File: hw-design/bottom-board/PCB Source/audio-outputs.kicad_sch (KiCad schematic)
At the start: 73 parts, among them J10 NYS215, J9 NYS215, K1 G6S-2, K2 G6S-2, Q1 2N7002, Q2 2N7002, U11 OPA1678, U12 OPA1678

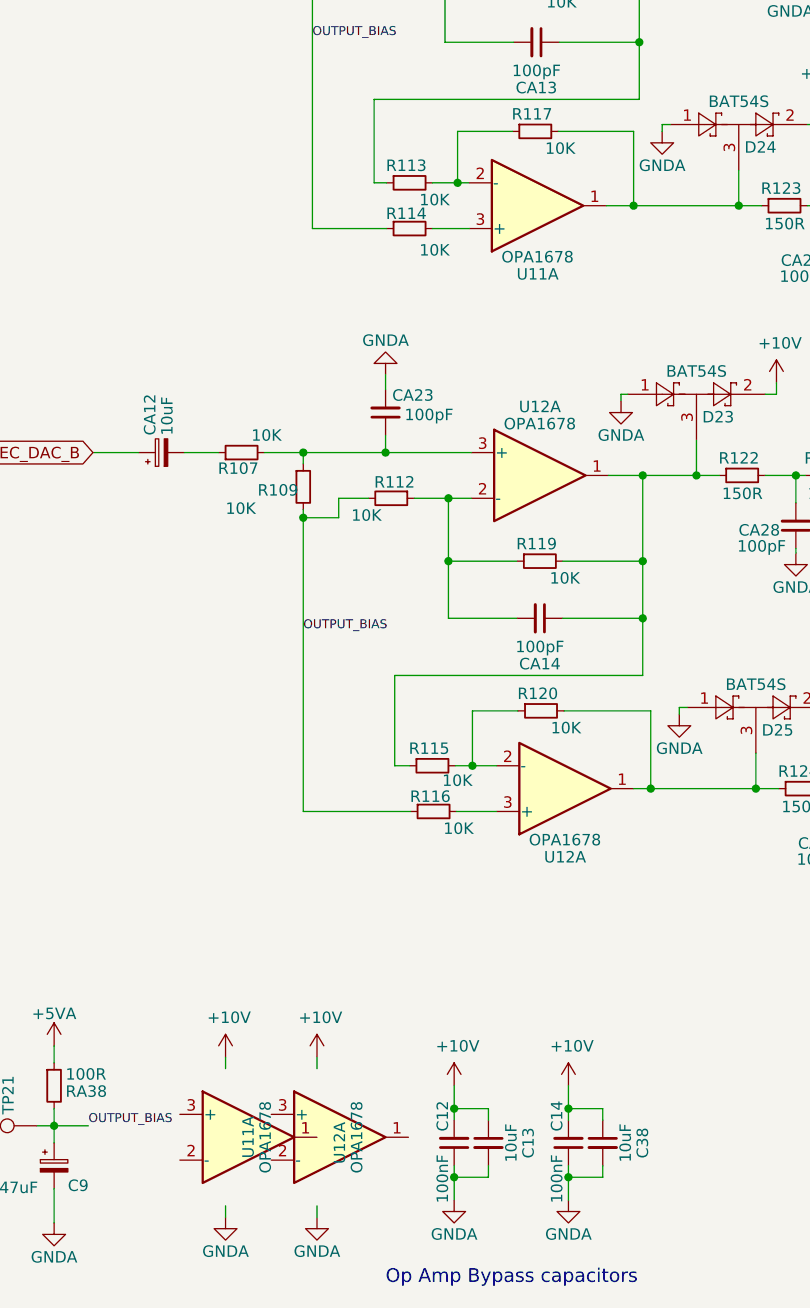
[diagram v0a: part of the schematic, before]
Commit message: change U21 (EXP supply) MPN, due to unavailabilaty again
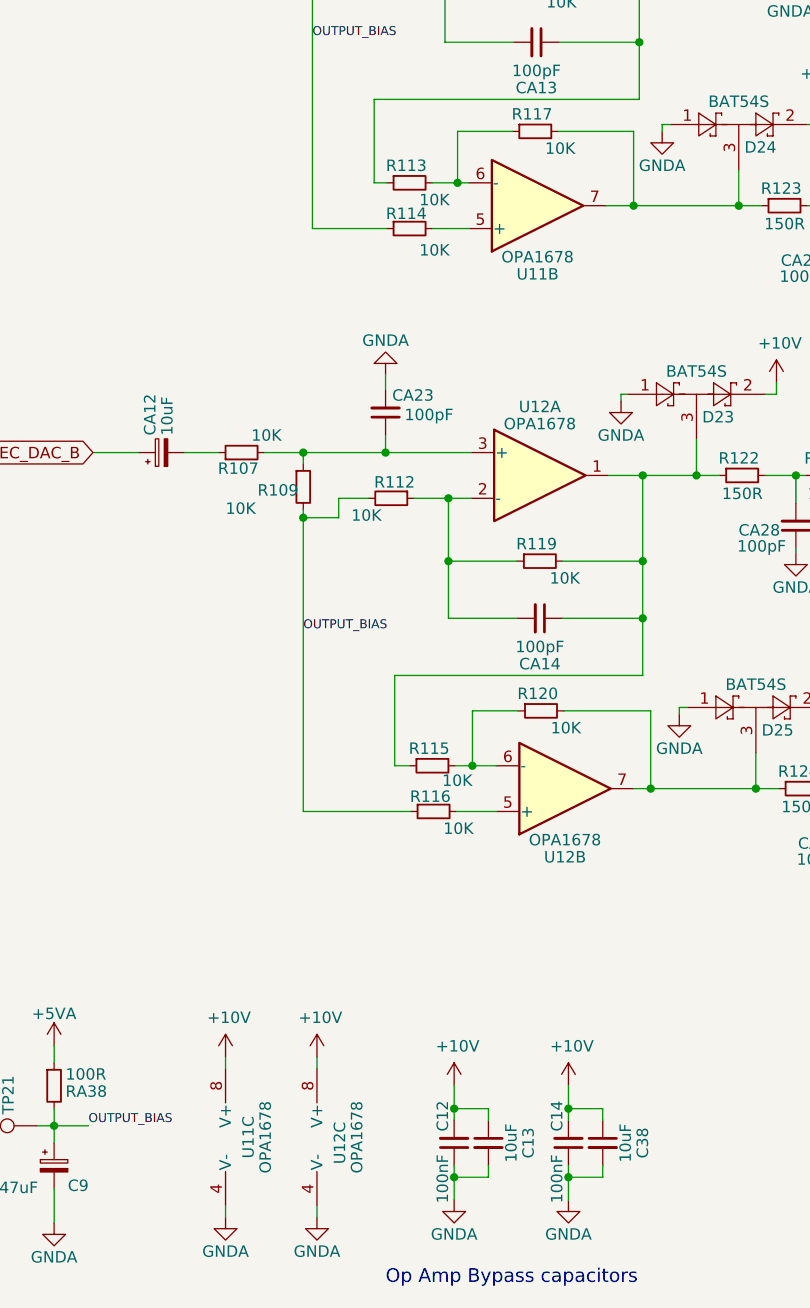
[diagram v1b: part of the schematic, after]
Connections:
- net +10V: now also U11.8 (V+), U12.8 (V+)
- net GNDA: now also U11.4 (V-), U12.4 (V-)
- net at D24.3, R117.2, R123.1: now also U11.7; no longer U11.1
- net at R113.2, R117.1: now also U11.6 (-); no longer U11.2 (-)
- net at R114.2: now also U11.5 (+); no longer U11.3 (+)
- net at D25.3, R120.2, R124.1: now also U12.7; no longer U12.1
- net at R115.2, R120.1: now also U12.6 (-); no longer U12.2 (-)
- net at R116.2: now also U12.5 (+); no longer U12.3 (+)
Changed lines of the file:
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@@
     (pin "3")
   )
-  (symbol (lib_id "bottom-board-rescue:LM4562-Amplifier_Operational") (at 45.085 168.91 0) (unit 1)
+  (symbol (lib_id "bottom-board-rescue:LM4562-Amplifier_Operational") (at 45.085 168.91 0) (unit 3)
     (in_bom yes) (on_board yes)
     (property "Reference" "U11" (id 0) (at 45.085 168.91 90))
@@
       (effects (font (size 1.27 1.27)) hide)
     )
-    (pin "1")
-    (pin "2")
-    (pin "3")
+    (pin "4")
+    (pin "8")
   )
   (symbol (lib_id "bottom-board-rescue:G6S-2-Relay") (at 154.813 108.077 90) (unit 1)
@@
     (pin "9")
   )
-  (symbol (lib_id "bottom-board-rescue:LM4562-Amplifier_Operational") (at 77.216 65.405 0) (mirror x) (unit 1)
+  (symbol (lib_id "bottom-board-rescue:LM4562-Amplifier_Operational") (at 77.216 65.405 0) (mirror x) (unit 2)
     (in_bom yes) (on_board yes)
     (property "Reference" "U11" (id 0) (at 77.216 73.025 0))
@@
       (effects (font (size 1.27 1.27)) hide)
     )
-    (pin "1")
-    (pin "2")
-    (pin "3")
+    (pin "5")
+    (pin "6")
+    (pin "7")
   )
-  (symbol (lib_id "bottom-board-rescue:LM4562-Amplifier_Operational") (at 55.245 168.91 0) (unit 1)
+  (symbol (lib_id "bottom-board-rescue:LM4562-Amplifier_Operational") (at 55.245 168.91 0) (unit 3)
     (in_bom yes) (on_board yes)
     (property "Reference" "U12" (id 0) (at 55.245 169.545 90))
@@
       (effects (font (size 1.27 1.27)) hide)
     )
-    (pin "1")
-    (pin "2")
-    (pin "3")
+    (pin "4")
+    (pin "8")
   )
   (symbol (lib_id "bottom-board-rescue:LM4562-Amplifier_Operational") (at 77.47 95.377 0) (unit 1)
@@
     (pin "3")
   )
-  (symbol (lib_id "bottom-board-rescue:LM4562-Amplifier_Operational") (at 80.264 130.175 0) (mirror x) (unit 1)
+  (symbol (lib_id "bottom-board-rescue:LM4562-Amplifier_Operational") (at 80.264 130.175 0) (mirror x) (unit 2)
     (in_bom yes) (on_board yes)
     (property "Reference" "U12" (id 0) (at 80.264 137.795 0))
@@
       (effects (font (size 1.27 1.27)) hide)
     )
-    (pin "1")
-    (pin "2")
-    (pin "3")
+    (pin "5")
+    (pin "6")
+    (pin "7")
   )
   (symbol (lib_id "bottom-board-rescue:R_Small-Device") (at 46.99 28.829 90) (unit 1)

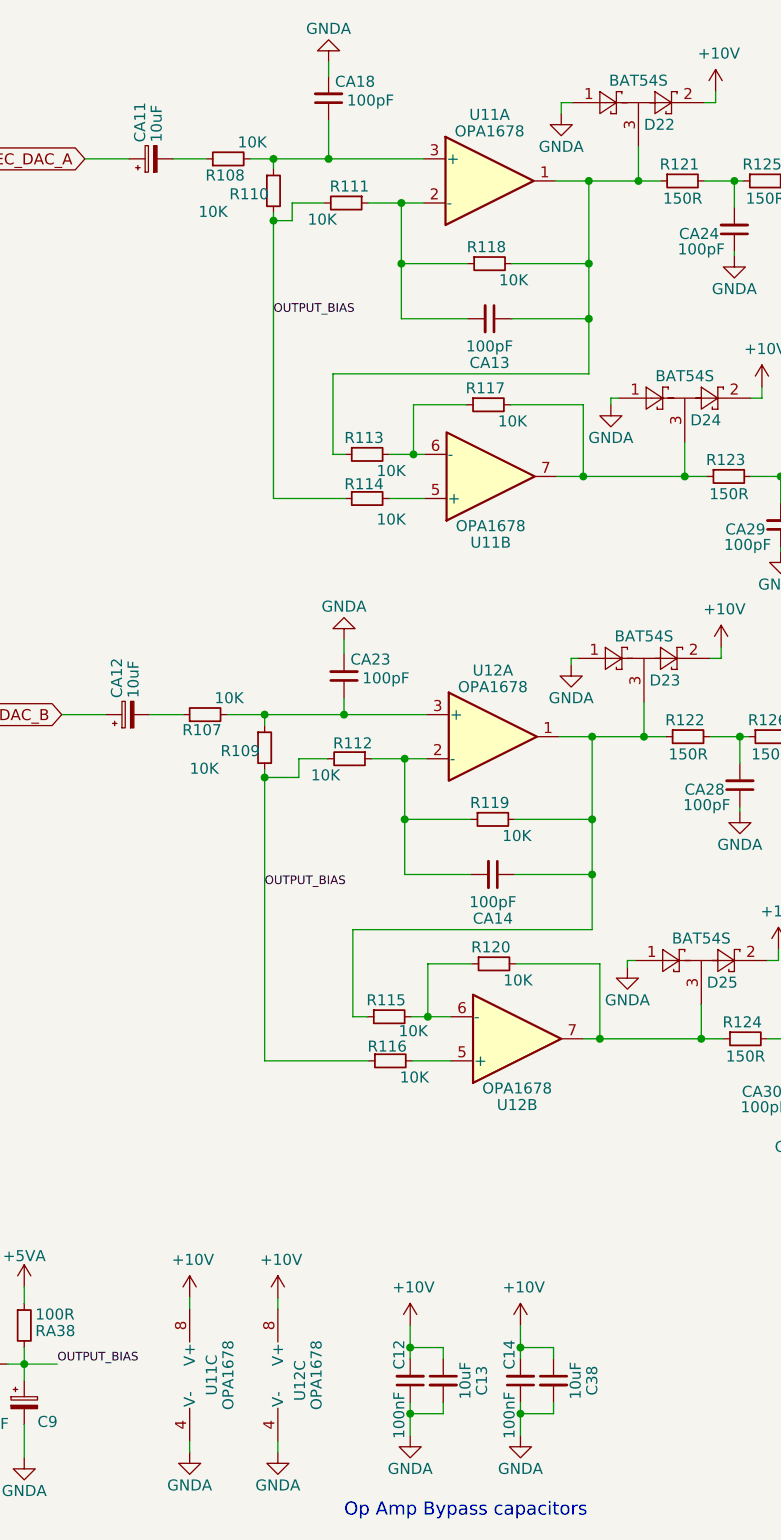
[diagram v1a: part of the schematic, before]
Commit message: change output opamps for the same reason
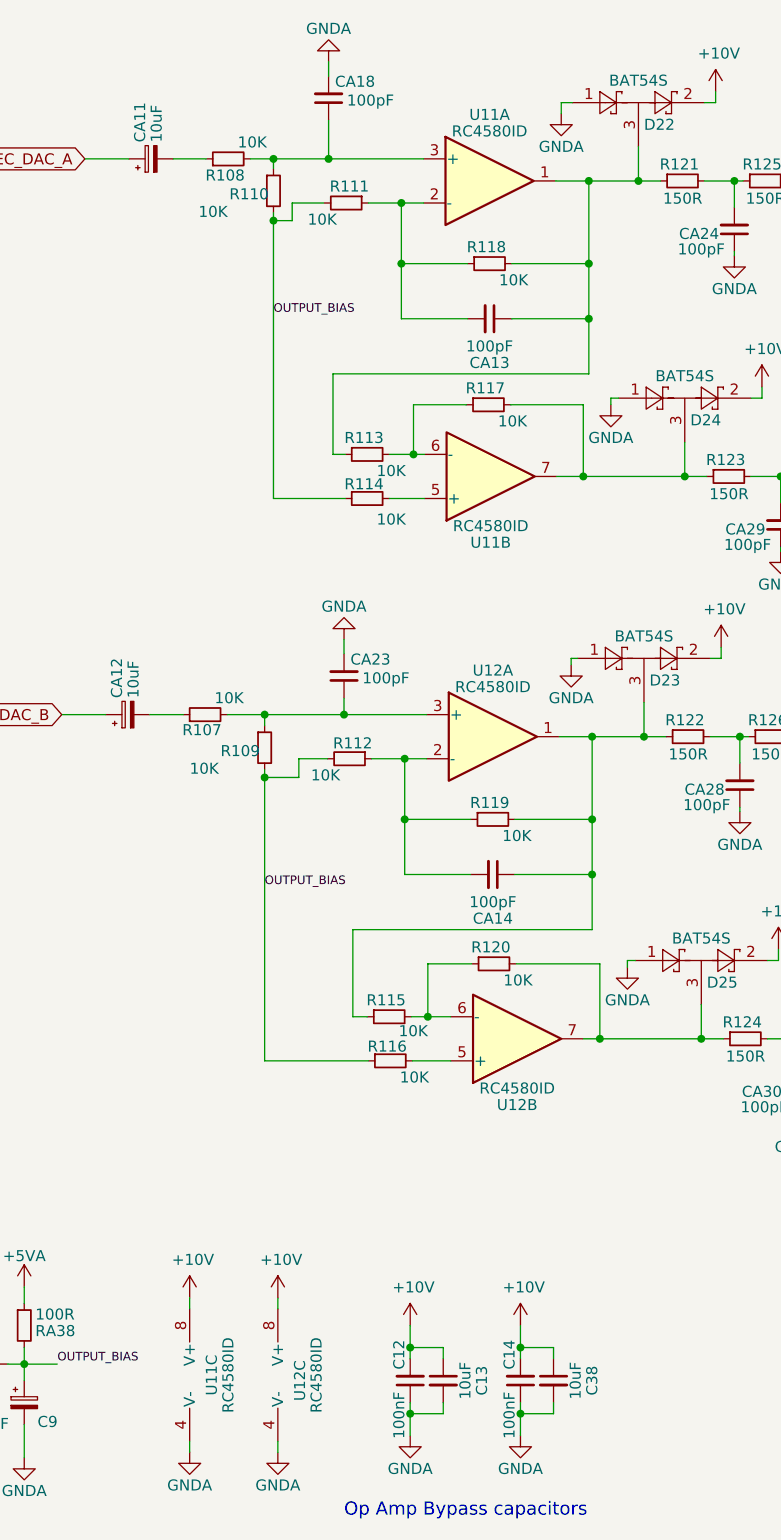
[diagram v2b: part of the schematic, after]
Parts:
- U11, U12: value OPA1678 -> RC4580ID
- U11, U12: value OPA1678 -> RC4580ID; MPN OPA1678IDR -> RC4580ID
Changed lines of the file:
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@@
     (in_bom yes) (on_board yes)
     (property "Reference" "U11" (id 0) (at 77.089 23.749 0))
-    (property "Value" "OPA1678" (id 1) (at 77.089 25.654 0))
+    (property "Value" "RC4580ID" (id 1) (at 77.089 25.654 0))
     (property "Footprint" "Package_SO:SOIC-8_3.9x4.9mm_P1.27mm" (id 2) (at 77.089 31.369 0)
       (effects (font (size 1.27 1.27)) hide)
@@
     (in_bom yes) (on_board yes)
     (property "Reference" "U11" (id 0) (at 45.085 168.91 90))
-    (property "Value" "OPA1678" (id 1) (at 46.99 168.91 90))
+    (property "Value" "RC4580ID" (id 1) (at 46.99 168.91 90))
     (property "Footprint" "Package_SO:SOIC-8_3.9x4.9mm_P1.27mm" (id 2) (at 45.085 168.91 0)
       (effects (font (size 1.27 1.27)) hide)
@@
     (in_bom yes) (on_board yes)
     (property "Reference" "U11" (id 0) (at 77.216 73.025 0))
-    (property "Value" "OPA1678" (id 1) (at 77.216 71.12 0))
+    (property "Value" "RC4580ID" (id 1) (at 77.216 71.12 0))
     (property "Footprint" "Package_SO:SOIC-8_3.9x4.9mm_P1.27mm" (id 2) (at 77.216 65.405 0)
       (effects (font (size 1.27 1.27)) hide)
@@
       (effects (font (size 1.27 1.27)) hide)
     )
-    (property "MPN" "OPA1678IDR" (id 4) (at -5.334 23.495 0)
+    (property "MPN" "RC4580ID" (id 4) (at -5.334 23.495 0)
       (effects (font (size 1.27 1.27)) hide)
     )
@@
     (in_bom yes) (on_board yes)
     (property "Reference" "U12" (id 0) (at 55.245 169.545 90))
-    (property "Value" "OPA1678" (id 1) (at 57.15 168.91 90))
+    (property "Value" "RC4580ID" (id 1) (at 57.15 168.91 90))
     (property "Footprint" "Package_SO:SOIC-8_3.9x4.9mm_P1.27mm" (id 2) (at 55.245 168.91 0)
       (effects (font (size 1.27 1.27)) hide)
@@
     (in_bom yes) (on_board yes)
     (property "Reference" "U12" (id 0) (at 77.47 87.757 0))
-    (property "Value" "OPA1678" (id 1) (at 77.47 89.662 0))
+    (property "Value" "RC4580ID" (id 1) (at 77.47 89.662 0))
     (property "Footprint" "Package_SO:SOIC-8_3.9x4.9mm_P1.27mm" (id 2) (at 77.47 95.377 0)
       (effects (font (size 1.27 1.27)) hide)
@@
     (in_bom yes) (on_board yes)
     (property "Reference" "U12" (id 0) (at 80.264 137.795 0))
-    (property "Value" "OPA1678" (id 1) (at 80.264 135.89 0))
+    (property "Value" "RC4580ID" (id 1) (at 80.264 135.89 0))
     (property "Footprint" "Package_SO:SOIC-8_3.9x4.9mm_P1.27mm" (id 2) (at 80.264 130.175 0)
       (effects (font (size 1.27 1.27)) hide)
@@
       (effects (font (size 1.27 1.27)) hide)
     )
-    (property "MPN" "OPA1678IDR" (id 4) (at -2.286 88.265 0)
+    (property "MPN" "RC4580ID" (id 4) (at -2.286 88.265 0)
       (effects (font (size 1.27 1.27)) hide)
     )

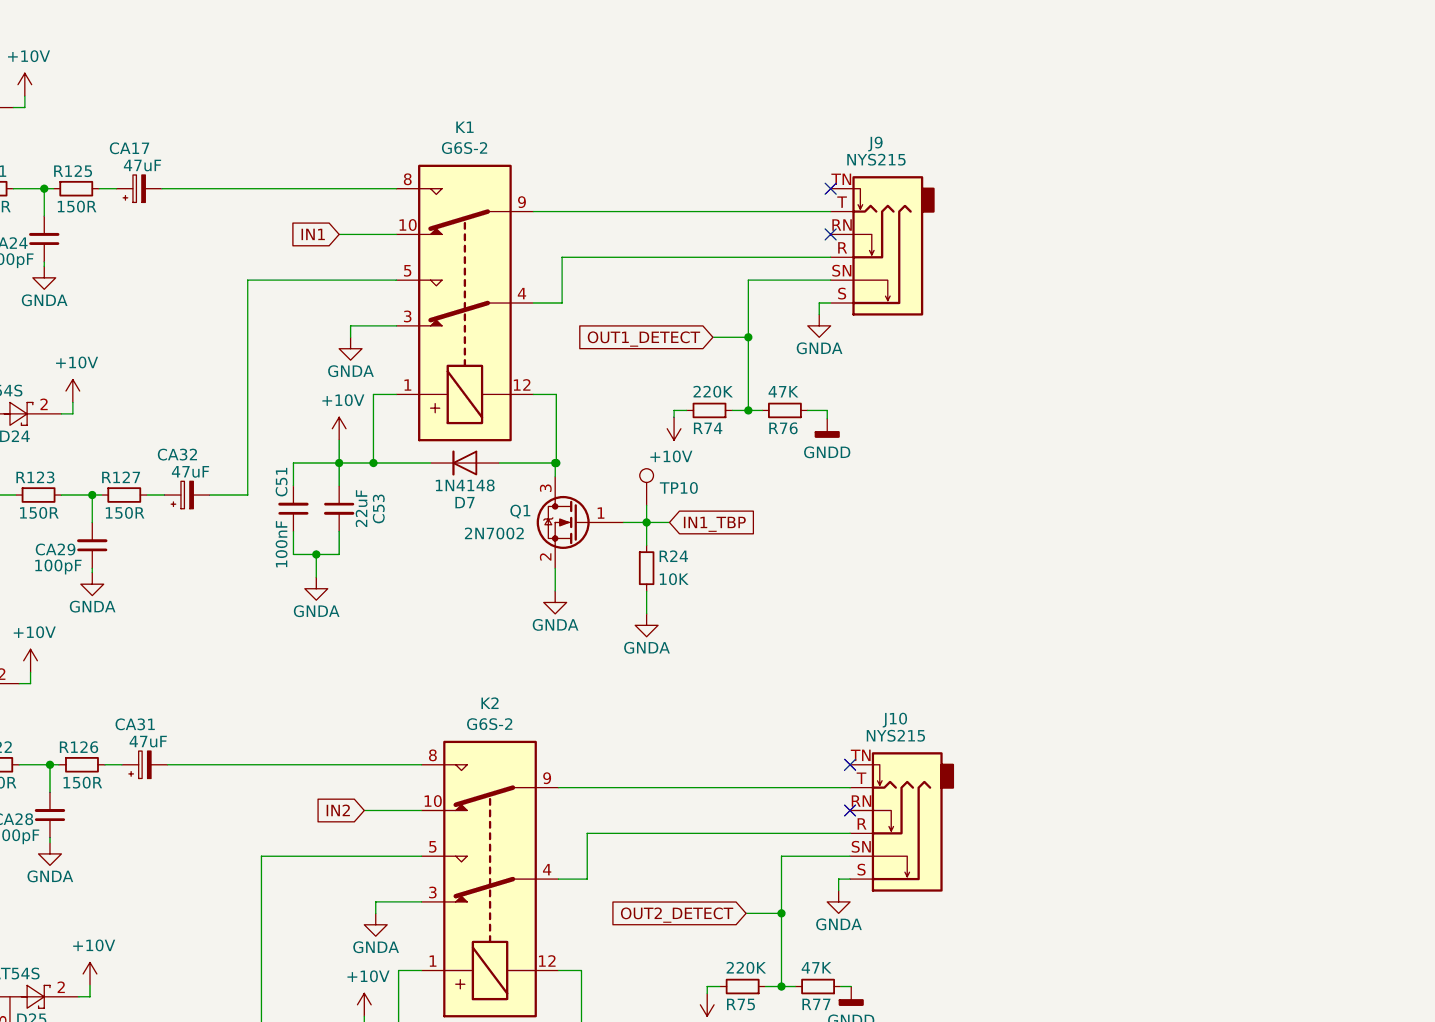
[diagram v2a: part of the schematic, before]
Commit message: make relay placement optional
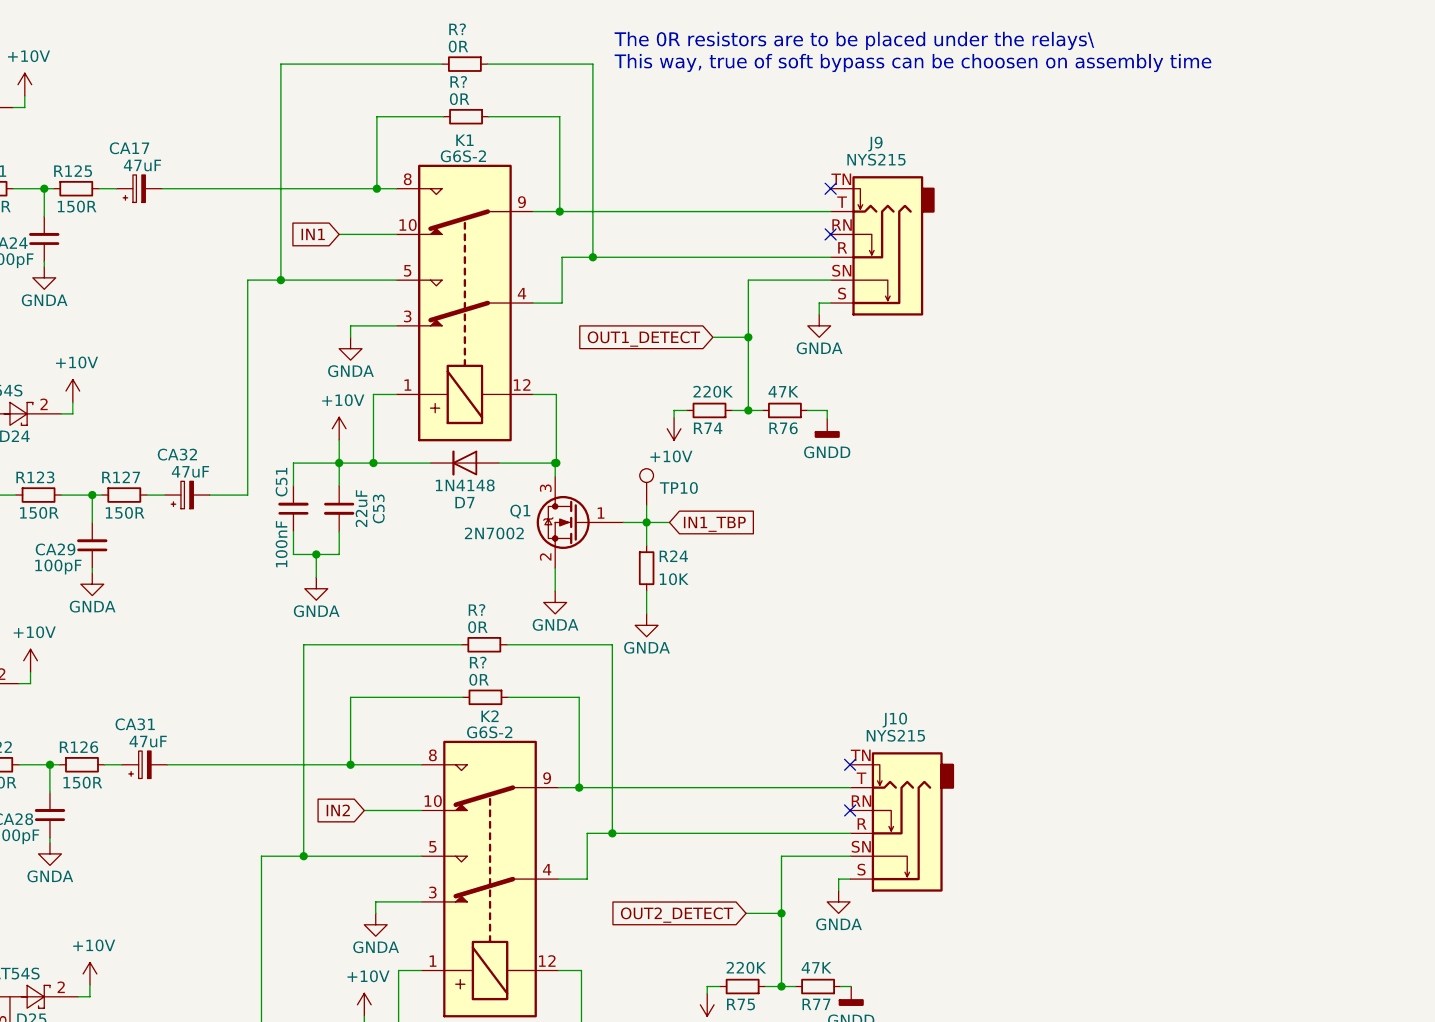
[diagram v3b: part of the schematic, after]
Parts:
- added R? (x4): 0R, Resistor_SMD:R_0603_1608Metric, symbol bottom-board-rescue:R_Small-Device
- C51, C52: MPN GCM188R71C104KA37D -> DO NOT PLACE
- C53, C54: MPN CL21A226MPQNNNE -> DO NOT PLACE
- D7: MPN 1N4148WX-TP -> NO DONT PLACE
- D8: MPN 1N4148WX-TP -> DO NOT PLACE
- K1, K2: MPN EE2-12NU-L -> DO NOT PLACE; MPN2 (none) -> EE2-12NU-L
- Q1, Q2: MPN 2N7002P,215 -> DO NOT PLACE
- R24, R25: MPN RR0816P-103-D -> DO NOT PLACE
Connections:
- net at CA17.2, K1.8: now also R?.2
- net at J9.R, K1.4: now also R?.1
- net at J9.T, K1.9: now also R?.1
- net at J10.R, K2.4: now also R?.1
- net at CA33.2, K2.5: now also R?.2
- net at CA31.2, K2.8: now also R?.2
- net at J10.T, K2.9: now also R?.1
- net at CA32.2, K1.5: now also R?.2
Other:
- note added: "The 0R resistors are to be placed under the relays\ This way, true of soft bypass can be choosen on assembly time"
